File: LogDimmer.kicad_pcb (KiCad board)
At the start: 2 copper layers, 19 parts, among them J1 Conn_01x02, J2 LED-PSU, J3 POT, U1 L78L33_SOT89, U2 PC817X3, U3 ATtiny13A-SS

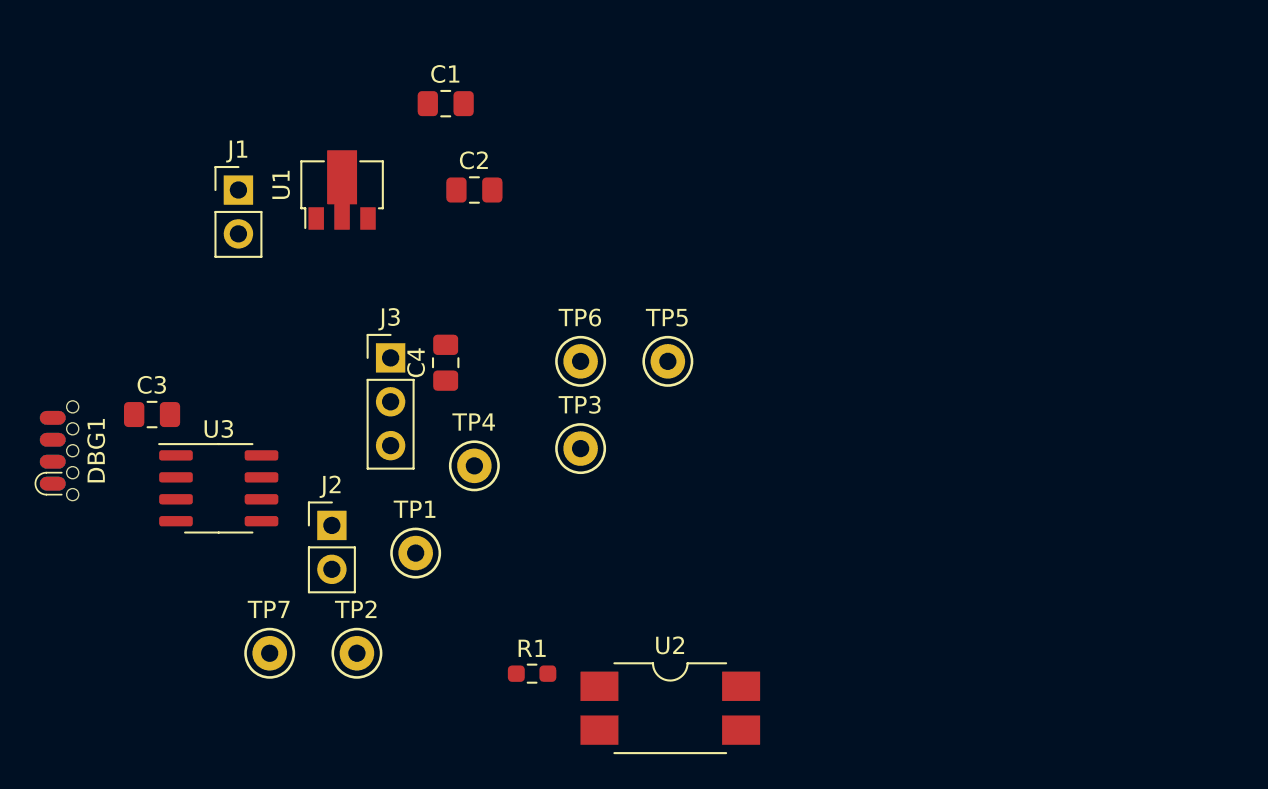
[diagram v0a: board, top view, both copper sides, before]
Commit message: Initial placements done. JRC design rules entered in project.
Design rule copper-to-hole limit dialled down to 0.2mm to allow for SOICbite breakout routing.
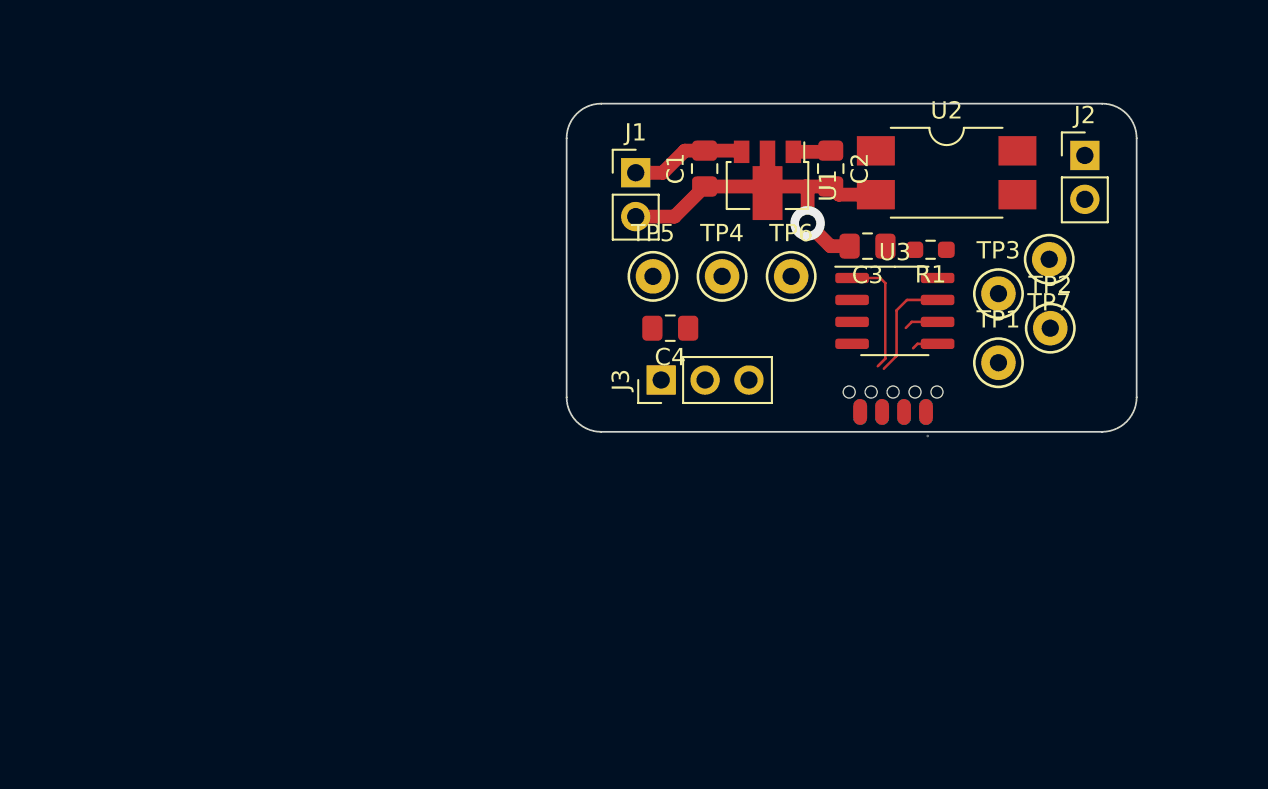
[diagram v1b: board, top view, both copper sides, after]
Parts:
- DBG1: moved to B.Cu
- moved TP7 50.6 mm to (177.9, 88.0), turned to 180 degrees
- moved DBG1 49.4 mm to (168.9, 97.6), turned to 180 degrees
- moved J2 48.6 mm to (180.0, 82.0)
- moved TP2 44.3 mm to (178.0, 92.0)
- moved C3 42.6 mm to (167.4, 87.2), turned to 180 degrees
- moved U3 40.5 mm to (169.0, 91.0)
- moved TP1 35.5 mm to (175.0, 94.0)
- moved U2 34.9 mm to (172.0, 83.0)
- moved R1 33.7 mm to (171.1, 87.5), turned to 180 degrees
- moved TP3 25.8 mm to (175.0, 90.0)
- moved U1 24.6 mm to (161.6, 83.4), turned to -90 degrees
- moved J1 23.0 mm to (154.0, 83.0)
- moved C2 20.7 mm to (165.3, 82.8), turned to -90 degrees
- moved TP4 18.1 mm to (159.0, 89.0)
- moved J3 15.7 mm to (155.5, 95.0), turned to 90 degrees
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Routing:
- net GND: track 0.00 -> 22.8 mm, vias 0 -> 1
- net ~{RST}: track 0.00 -> 7.04 mm
- net +5V: track 0.00 -> 6.69 mm
- net SCK: track 0.00 -> 6.31 mm
- net +3V3: track 0.00 -> 2.19 mm
- net MISO: track 0.00 -> 1.98 mm
- net MOSI: track 0.00 -> 1.52 mm
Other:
- board outline added: 33 x 19 mm

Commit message: Initial routing done
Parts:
- moved C4 3.30 mm to (159.3, 92.1)
- moved TP2 2.21 mm to (178.7, 94.1)
- moved TP7 1.69 mm to (178.6, 89.6)
- moved TP1 1.40 mm to (175.1, 95.4)
- moved C2 1.15 mm to (164.1, 82.8)
- moved U1 1.11 mm to (160.5, 83.5)
- moved C1 1.05 mm to (156.9, 82.8)
- moved C3 0.51 mm to (167.5, 87.8)
- moved R1 0.51 mm to (171.2, 88.0)
- moved U3 0.51 mm to (169.1, 91.5)
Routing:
- net +3V3: track 2.19 -> 49.6 mm, vias 0 -> 3
- net MOSI: track 1.52 -> 21.0 mm, vias 0 -> 1
- net Net-(C4-Pad2): track 0.00 -> 18.4 mm
- net MISO: track 1.98 -> 14.3 mm
- net Net-(R1-Pad2): track 0.00 -> 9.07 mm
- net Net-(TP4-Pad1): track 0.00 -> 8.43 mm
- net GND: track 22.8 -> 29.0 mm, vias 1 -> 3
- net ~{RST}: track 7.04 -> 13.2 mm
- net SCK: track 6.31 -> 12.3 mm
- net /DIM-: track 0.00 -> 4.01 mm
- net /DIM+: track 0.00 -> 4.01 mm
- net +5V: track 6.69 -> 5.55 mm
- added copper zone on B.Cu, net GND

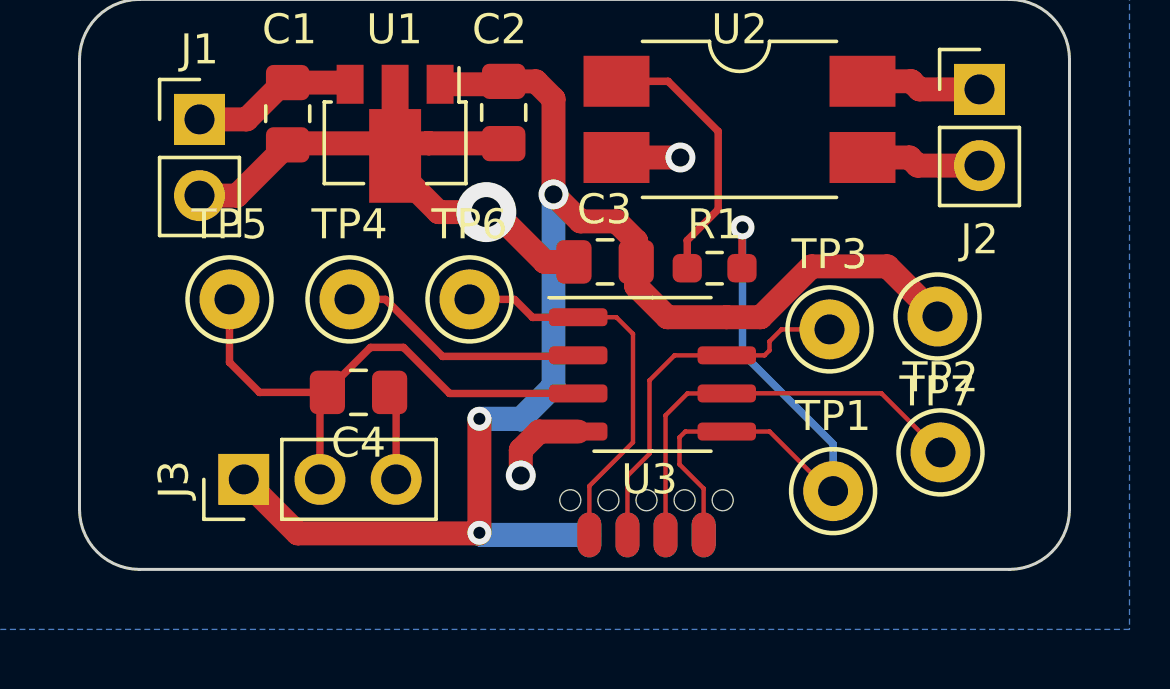
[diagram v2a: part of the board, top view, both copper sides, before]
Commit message: DRC clearing & silks
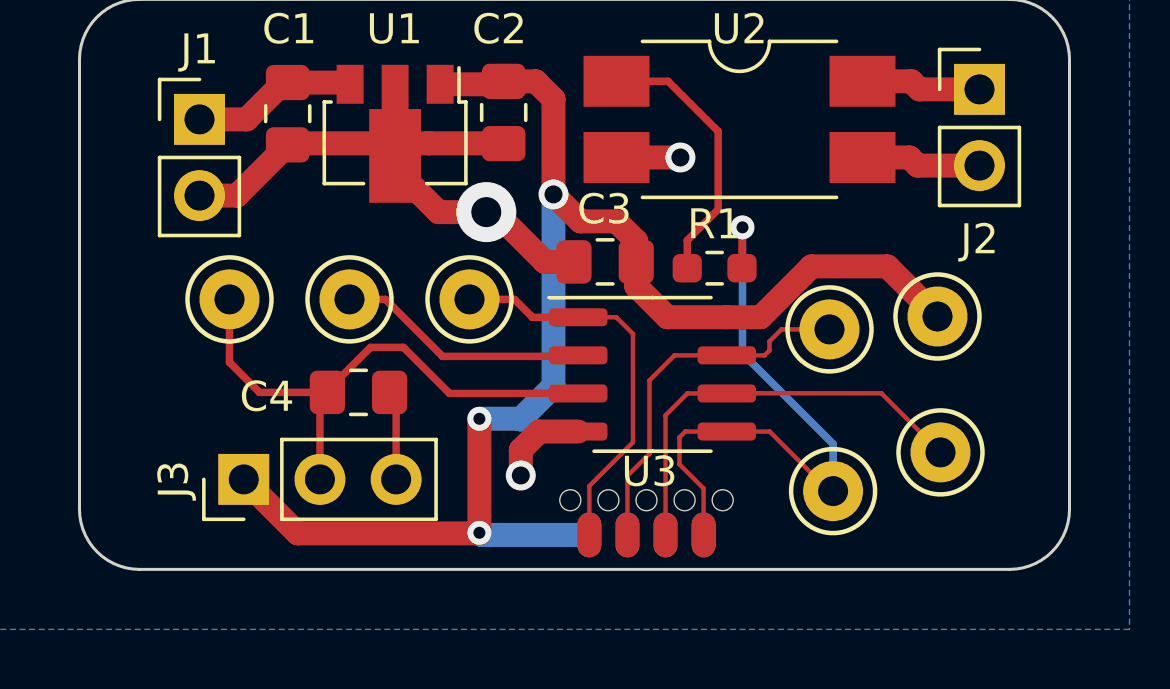
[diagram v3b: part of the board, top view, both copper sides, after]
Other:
- board text added: "LogDimmer BESearle 2022"
- board text added: "REV A"
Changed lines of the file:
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@@
     (property "Sheetname" "")
     (attr through_hole)
-    (fp_text reference "TP7" (at 0 -2.5) (layer "F.SilkS")
-      (effects (font (size 1 1) (thickness 0.15)))
-    )
-    (fp_text value "3V3" (at 0 2.5) (layer "F.Fab")
-      (effects (font (size 1 1) (thickness 0.15)))
+    (fp_text reference "TP7" (at 0 -2.5) (layer "User.1")
+      (effects (font (size 1 1) (thickness 0.15)))
+    )
+    (fp_text value "3V3" (at 1.85 1.57 315 unlocked) (layer "B.SilkS")
+      (effects (font (size 1 1) (thickness 0.15)) (justify mirror))
     )
     (fp_text user "${REFERENCE}" (at 0 -2.5) (layer "F.Fab")
@@
     (property "Sheetname" "")
     (attr through_hole)
-    (fp_text reference "TP2" (at 0 -2.5) (layer "F.SilkS")
-      (effects (font (size 1 1) (thickness 0.15)))
-    )
-    (fp_text value "PB1" (at 0 2.5) (layer "F.Fab")
-      (effects (font (size 1 1) (thickness 0.15)))
+    (fp_text reference "TP2" (at 0 -2.5) (layer "User.1")
+      (effects (font (size 1 1) (thickness 0.15)))
+    )
+    (fp_text value "PB1" (at -1.95 -1.85 -45 unlocked) (layer "B.SilkS")
+      (effects (font (size 1 1) (thickness 0.15)) (justify mirror))
     )
     (fp_text user "${REFERENCE}" (at 0 -2.5) (layer "F.Fab")
@@
     (property "Sheetname" "")
     (attr smd)
-    (fp_text reference "U3" (at -0.1 3.5 180) (layer "F.SilkS")
+    (fp_text reference "U3" (at -0.1 3.25 180) (layer "F.SilkS")
       (effects (font (size 1 1) (thickness 0.15)))
     )
@@
     (property "Sheetname" "")
     (attr through_hole)
-    (fp_text reference "TP3" (at 0 -2.5) (layer "F.SilkS")
-      (effects (font (size 1 1) (thickness 0.15)))
-    )
-    (fp_text value "PB2" (at 0 2.5) (layer "F.Fab")
-      (effects (font (size 1 1) (thickness 0.15)))
+    (fp_text reference "TP3" (at 0 -2.5) (layer "User.1")
+      (effects (font (size 1 1) (thickness 0.15)))
+    )
+    (fp_text value "PB2" (at -2 -1.75 -45 unlocked) (layer "B.SilkS")
+      (effects (font (size 1 1) (thickness 0.15)) (justify mirror))
     )
     (fp_text user "${REFERENCE}" (at 0 -2.5) (layer "F.Fab")
@@
     (property "Sheetname" "")
     (attr through_hole)
-    (fp_text reference "TP6" (at 0 -2.5) (layer "F.SilkS")
-      (effects (font (size 1 1) (thickness 0.15)))
-    )
-    (fp_text value "PB5" (at 0 2.5) (layer "F.Fab")
-      (effects (font (size 1 1) (thickness 0.15)))
+    (fp_text reference "TP6" (at 0 -2.5) (layer "User.1")
+      (effects (font (size 1 1) (thickness 0.15)))
+    )
+    (fp_text value "PB5" (at -2 -2 -45 unlocked) (layer "B.SilkS")
+      (effects (font (size 1 1) (thickness 0.15)) (justify mirror))
     )
     (fp_text user "${REFERENCE}" (at -0.3 -2.51) (layer "F.Fab")
@@
     (property "Sheetname" "")
     (attr through_hole)
-    (fp_text reference "TP1" (at 0 -2.5) (layer "F.SilkS")
-      (effects (font (size 1 1) (thickness 0.15)))
-    )
-    (fp_text value "PB0" (at 0 2.5) (layer "F.Fab")
-      (effects (font (size 1 1) (thickness 0.15)))
+    (fp_text reference "TP1" (at 0 -2.5) (layer "User.1")
+      (effects (font (size 1 1) (thickness 0.15)))
+    )
+    (fp_text value "PB0" (at -2.12 -1.89 -45 unlocked) (layer "B.SilkS")
+      (effects (font (size 1 1) (thickness 0.15)) (justify mirror))
     )
     (fp_text user "${REFERENCE}" (at 0 -2.5) (layer "F.Fab")
@@
     (property "Sheetname" "")
     (attr smd)
-    (fp_text reference "C4" (at 0 -1.68) (layer "F.SilkS")
+    (fp_text reference "C4" (at 3.05 -0.15) (layer "F.SilkS")
       (effects (font (size 1 1) (thickness 0.15)))
     )
@@
     (property "Sheetname" "")
     (attr through_hole)
-    (fp_text reference "TP4" (at 0 -2.5) (layer "F.SilkS")
-      (effects (font (size 1 1) (thickness 0.15)))
-    )
-    (fp_text value "PB3" (at 0 2.5) (layer "F.Fab")
-      (effects (font (size 1 1) (thickness 0.15)))
+    (fp_text reference "TP4" (at 0 -2.5) (layer "User.1")
+      (effects (font (size 1 1) (thickness 0.15)))
+    )
+    (fp_text value "PB3" (at -2 -2 -45 unlocked) (layer "B.SilkS")
+      (effects (font (size 1 1) (thickness 0.15)) (justify mirror))
     )
     (fp_text user "${REFERENCE}" (at 0 -2.5) (layer "F.Fab")
@@
     (property "Sheetname" "")
     (attr through_hole)
-    (fp_text reference "TP5" (at 0 -2.5) (layer "F.SilkS")
-      (effects (font (size 1 1) (thickness 0.15)))
-    )
-    (fp_text value "PB4" (at 0 2.5) (layer "F.Fab")
-      (effects (font (size 1 1) (thickness 0.15)))
+    (fp_text reference "TP5" (at 0 -2.5) (layer "User.1")
+      (effects (font (size 1 1) (thickness 0.15)))
+    )
+    (fp_text value "PB4" (at 2 2 -45 unlocked) (layer "B.SilkS")
+      (effects (font (size 1 1) (thickness 0.15)) (justify mirror))
     )
     (fp_text user "${REFERENCE}" (at 0 -2.5) (layer "F.Fab")
@@
       (net 11 "~{RST}") (pinfunction "~{RST}") (pintype "output"))
   )
+  (gr_line (start 165.5 84.625) (end 155.5 84.625) (layer "B.SilkS") (width 0.4))
+  (gr_line (start 155.5 84.625) (end 155.5 80.375) (layer "B.SilkS") (width 0.4))
+  (gr_line (start 155.5 80.375) (end 165.5 80.375) (layer "B.SilkS") (width 0.4))
+  (gr_line (start 165.5 80.375) (end 165.5 84.625) (layer "B.SilkS") (width 0.4))
   (gr_arc (start 152 98) (mid 150.585786 97.414214) (end 150 96) (layer "Edge.Cuts") (width 0.1))
   (gr_line (start 183 81) (end 183 96) (layer "Edge.Cuts") (width 0.1))
@@
   (gr_line (start 150 96) (end 150 81) (layer "Edge.Cuts") (width 0.1))
   (gr_arc (start 183 96) (mid 182.414214 97.414214) (end 181 98) (layer "Edge.Cuts") (width 0.1))
+  (gr_text "LogDimmer\nBESearle 2022" (at 178.25 82.75) (layer "B.SilkS")
+    (effects (font (size 1.5 1) (thickness 0.25)) (justify left mirror))
+  )
+  (gr_text "REV A" (at 165.25 82.625) (layer "B.SilkS")
+    (effects (font (size 2.5 2) (thickness 0.4)) (justify left mirror))
+  )
   (dimension (type aligned) (layer "F.Fab")
     (pts (xy 181 79) (xy 181 98))
@@
   (via (at 163.33 96.78) (size 0.8) (drill 0.4) (layers "F.Cu" "B.Cu") (net 3))
   (via (at 163.33 92.98) (size 0.8) (drill 0.4) (layers "F.Cu" "B.Cu") (net 3))
-  (segment (start 165.88 85.42) (end 165.8 85.5) (width 0.8) (layer "B.Cu") (net 3))
   (segment (start 164.68 92.98) (end 164.7 93) (width 0.8) (layer "B.Cu") (net 3))
   (segment (start 165.8 91.9) (end 164.7 93) (width 0.8) (layer "B.Cu") (net 3))
-  (segment (start 165.8 85.5) (end 165.8 91.9) (width 0.8) (layer "B.Cu") (net 3))
   (segment (start 163.4 96.85) (end 163.33 96.78) (width 0.8) (layer "B.Cu") (net 3))
   (segment (start 163.33 92.98) (end 164.68 92.98) (width 0.8) (layer "B.Cu") (net 3))
+  (segment (start 165.8 85.5) (end 165.8 91.9) (width 0.8) (layer "B.Cu") (net 3))
   (segment (start 166.995 96.85) (end 163.4 96.85) (width 0.8) (layer "B.Cu") (net 3))
   (segment (start 160.8 90.6) (end 162.335 92.135) (width 0.25) (layer "F.Cu") (net 4))
@@
   (segment (start 176.73 92.13) (end 178.7 94.1) (width 0.15) (layer "F.Cu") (net 5))
   (segment (start 170.265 92.135) (end 169.535 92.865) (width 0.15) (layer "F.Cu") (net 5))
+  (segment (start 170.265 92.135) (end 171.575 92.135) (width 0.15) (layer "F.Cu") (net 5))
   (segment (start 169.535 92.865) (end 169.535 96.85) (width 0.15) (layer "F.Cu") (net 5))
-  (segment (start 171.575 92.135) (end 170.265 92.135) (width 0.15) (layer "F.Cu") (net 5))
-  (segment (start 171.61 92.1) (end 171.575 92.135) (width 0.15) (layer "F.Cu") (net 5))
-  (segment (start 171.575 92.135) (end 171.58 92.13) (width 0.15) (layer "F.Cu") (net 5))
-  (segment (start 171.58 92.13) (end 176.73 92.13) (width 0.15) (layer "F.Cu") (net 5))
+  (segment (start 171.58 92.13) (end 171.575 92.135) (width 0.15) (layer "F.Cu") (net 5))
+  (segment (start 176.73 92.13) (end 171.58 92.13) (width 0.15) (layer "F.Cu") (net 5))
   (segment (start 172.0825 87.96) (end 172.0825 86.6175) (width 0.25) (layer "F.Cu") (net 6))
   (segment (start 170.805 95.305) (end 170.805 96.85) (width 0.15) (layer "F.Cu") (net 6))
